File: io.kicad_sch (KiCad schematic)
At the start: 2 parts, among them J4 JST XH, J5 JST XH

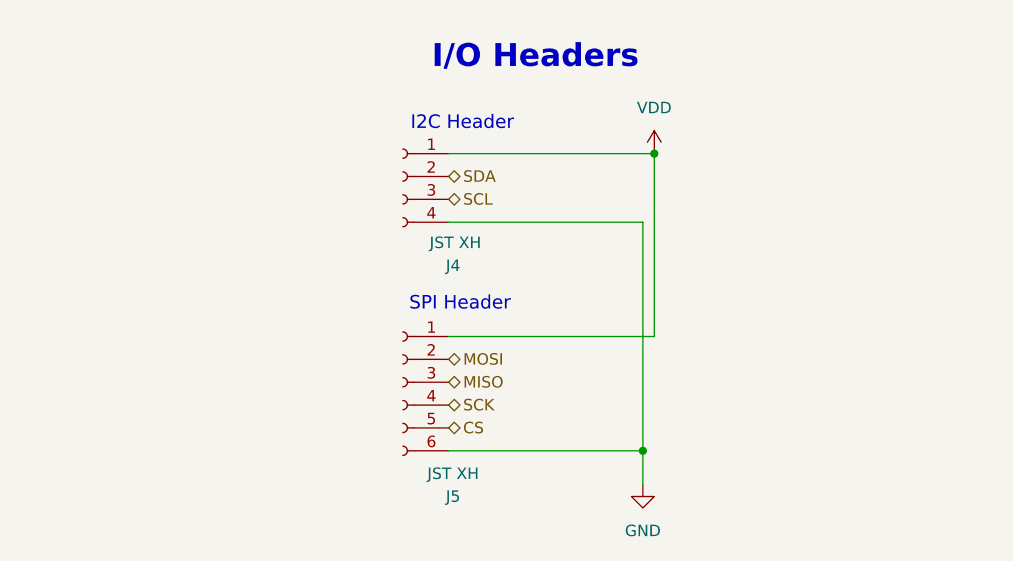
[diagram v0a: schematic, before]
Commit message: v2.2 with added indicator LEDs and a user button
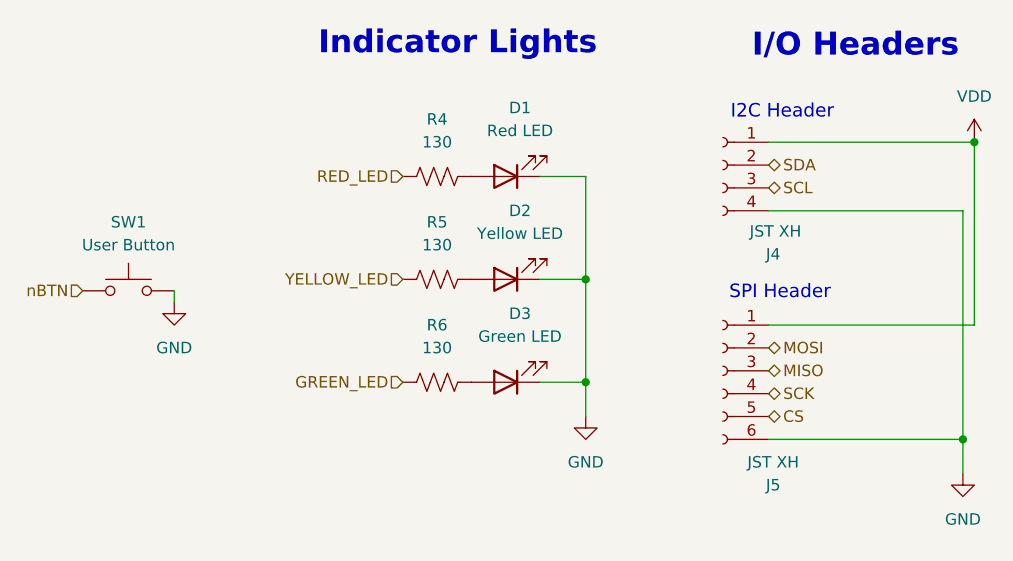
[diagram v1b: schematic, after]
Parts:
- added D1: Red LED, LED_SMD:LED_1206_3216Metric, symbol Device:LED
- added D2: Yellow LED, LED_SMD:LED_1206_3216Metric, symbol Device:LED
- added D3: Green LED, LED_SMD:LED_1206_3216Metric, symbol Device:LED
- added R4, R5, R6: 130, Resistor_SMD:R_0805_2012Metric, symbol Device:R_US
- added SW1: User Button, Button_Switch_THT:SW_PUSH_6mm, symbol Switch:SW_Push
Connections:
- net GND: now also D1.1 (K), D2.1 (K), D3.1 (K), SW1.2
- new net: D3.2 (A), R6.2
- new net: D1.2 (A), R4.2
- new net: D2.2 (A), R5.2
- new net GREEN_LED: R6.1
- new net RED_LED: R4.1
- new net YELLOW_LED: R5.1
- new net nBTN: SW1.1
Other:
- note added: "Indicator Lights"
- moved on the sheet: J4, J5
